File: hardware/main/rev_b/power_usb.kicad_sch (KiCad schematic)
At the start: 32 parts, among them J1 USB-C USB2, J2 ESC_CAN_POWER, U1 USBLC6-2SC6, U2 TLV62569DBVR, U3 TLV75528PDBVR, U4 TLV75533PDBVR

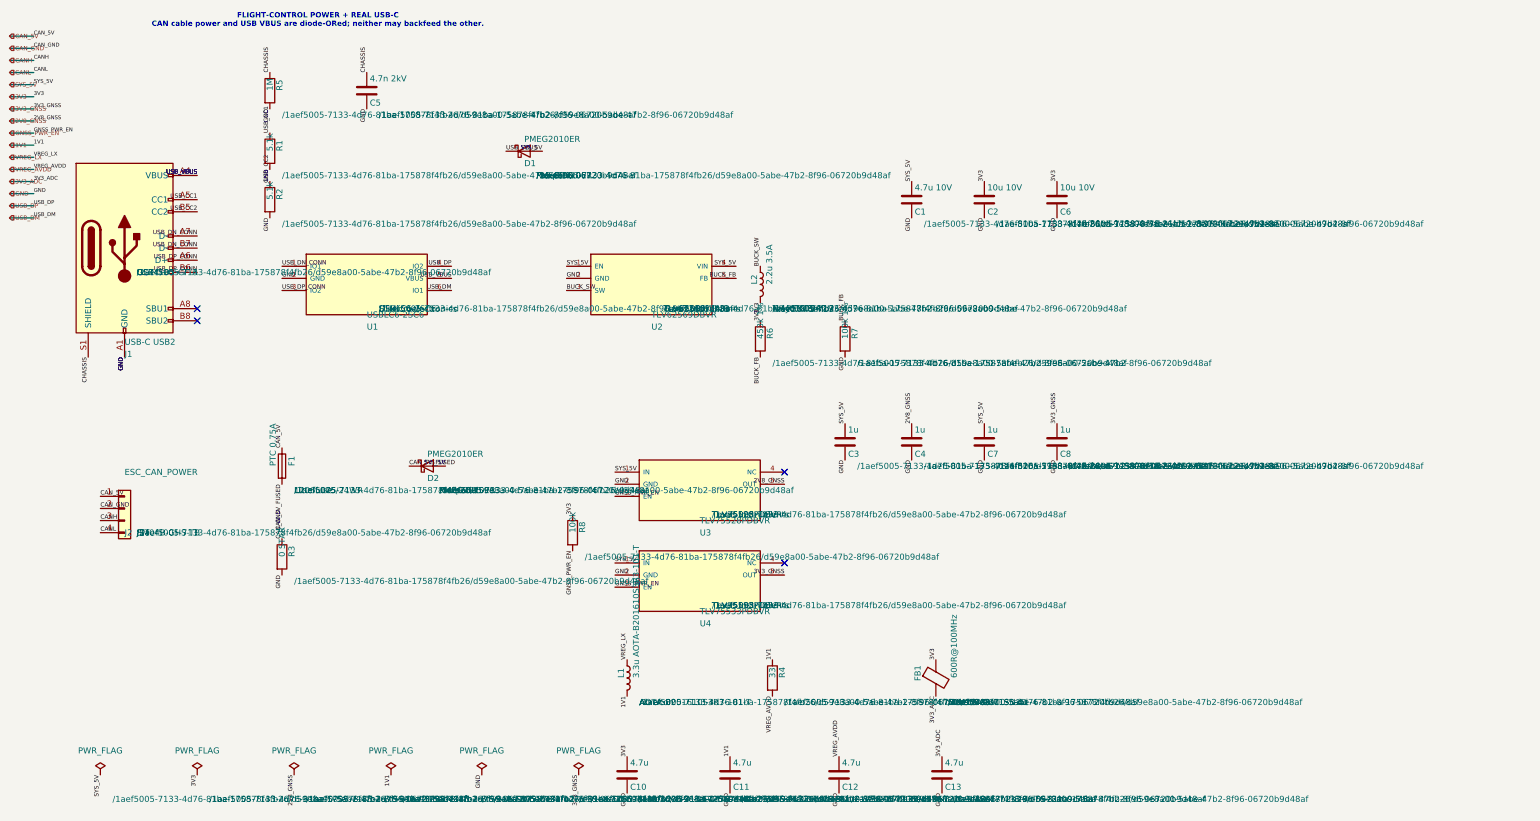
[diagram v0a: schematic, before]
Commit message: build: route and validate rev-b boards
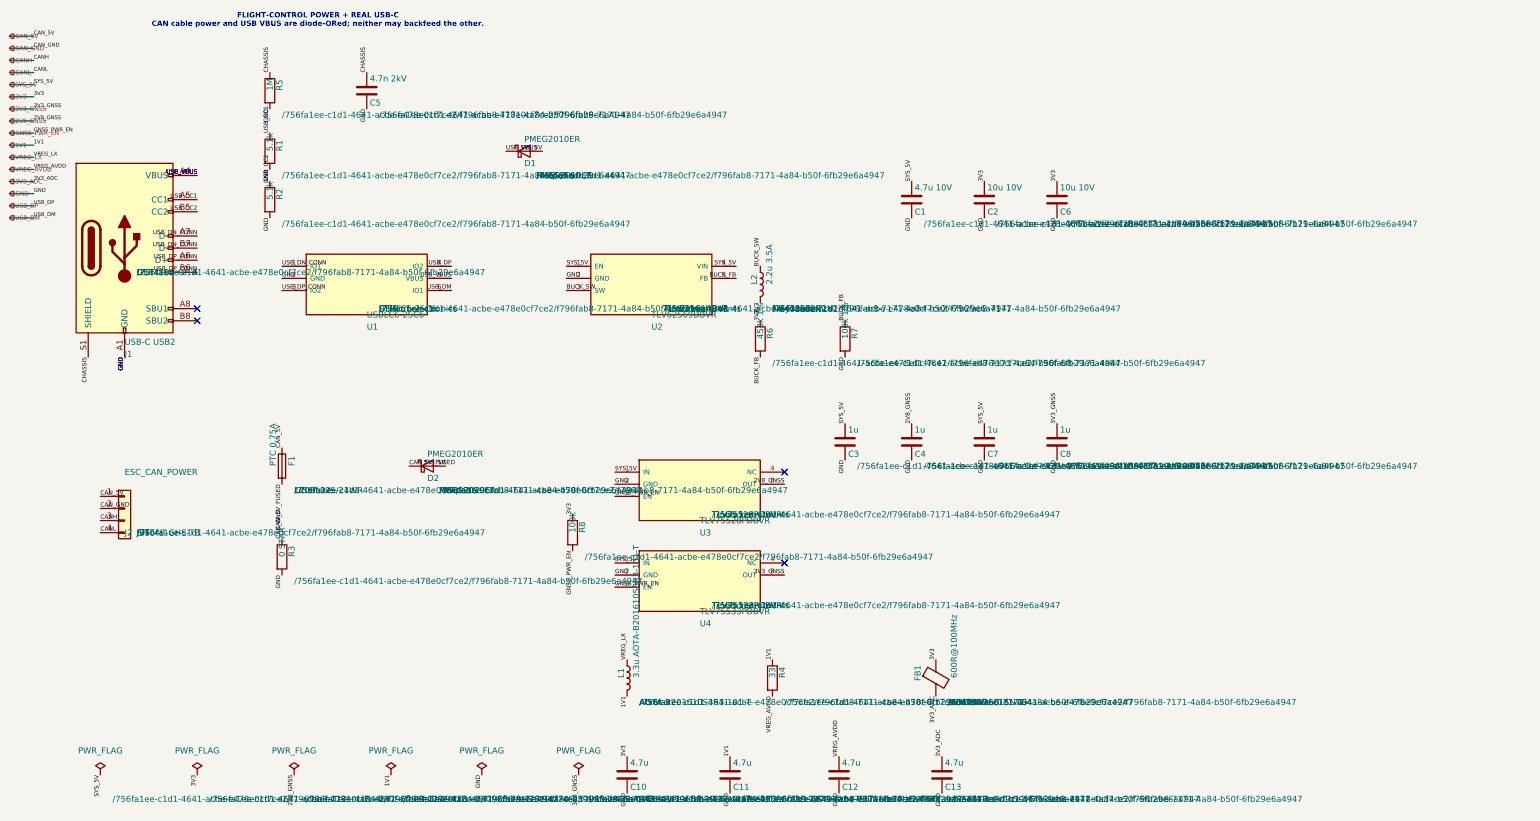
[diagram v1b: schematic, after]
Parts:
- C1, C10, C11, C12, C13, C2, C3, C4, C5, C6, C7, C8, D1, D2, F1, FB1, J1, J2, L1, L2, R1, R2, R3, R4, R5, R6, R7, R8, U1, U2, U3, U4: hierarchy_path /1aef5005-7133-4d76-81ba-175878f4fb26/d59e8a00-5abe-47b2-8f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 -> /756fa1ee-c1d1-4641-acbe-e478e0cf7ce2/f796fab8-7171-4a84-b5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

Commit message: build: route and validate rev-b boards
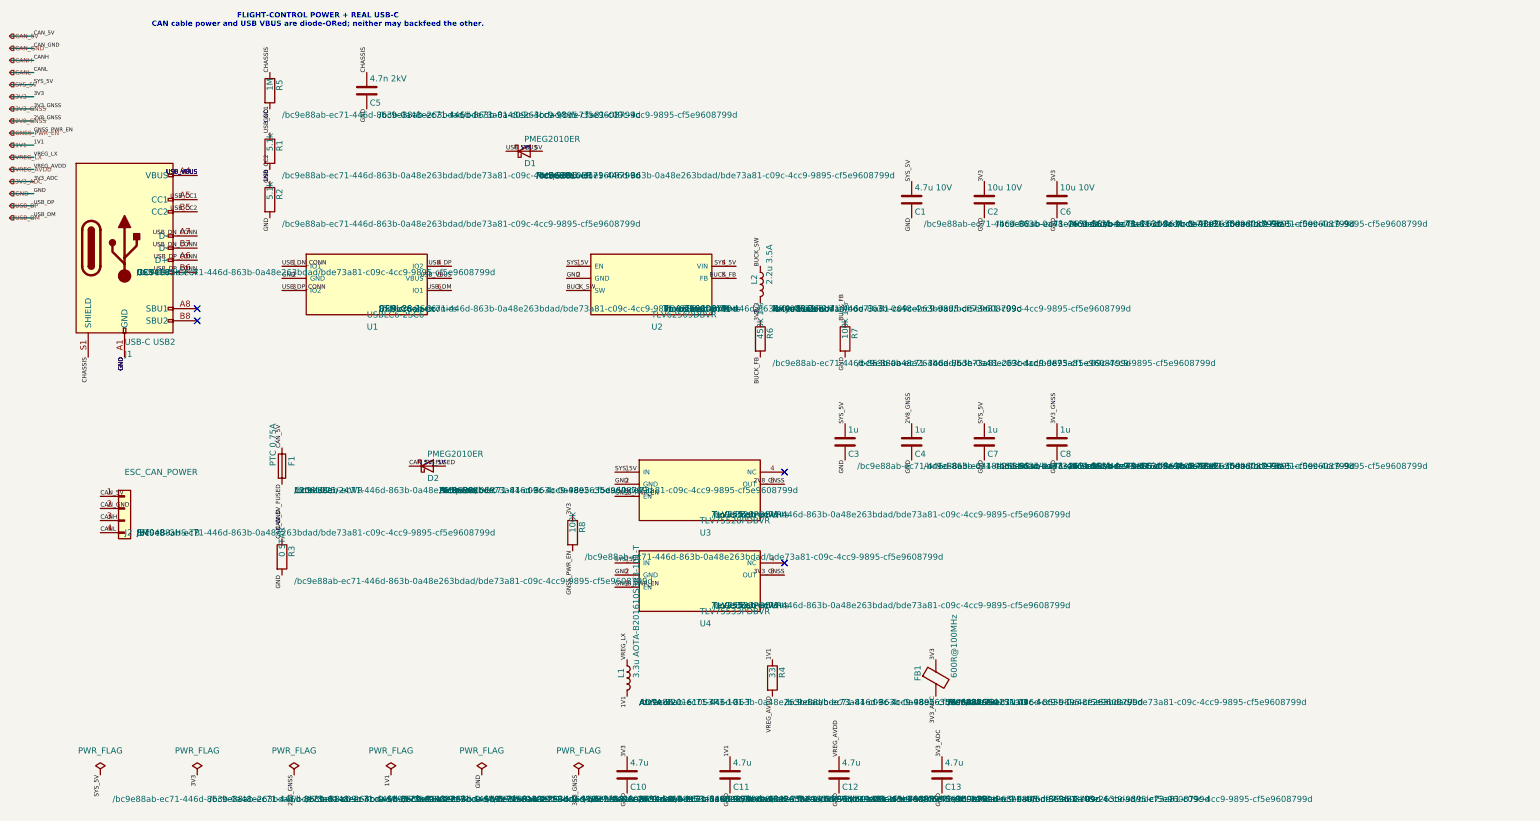
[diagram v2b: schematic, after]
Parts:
- C1, C10, C11, C12, C13, C2, C3, C4, C5, C6, C7, C8, D1, D2, F1, FB1, J1, J2, L1, L2, R1, R2, R3, R4, R5, R6, R7, R8, U1, U2, U3, U4: hierarchy_path /756fa1ee-c1d1-4641-acbe-e478e0cf7ce2/f796fab8-7171-4a84-b5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 -> /bc9e88ab-ec71-446d-863b-0a48e263bdad/bde73a81-c09c-4cc9-98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

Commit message: build: route and validate rev-b boards
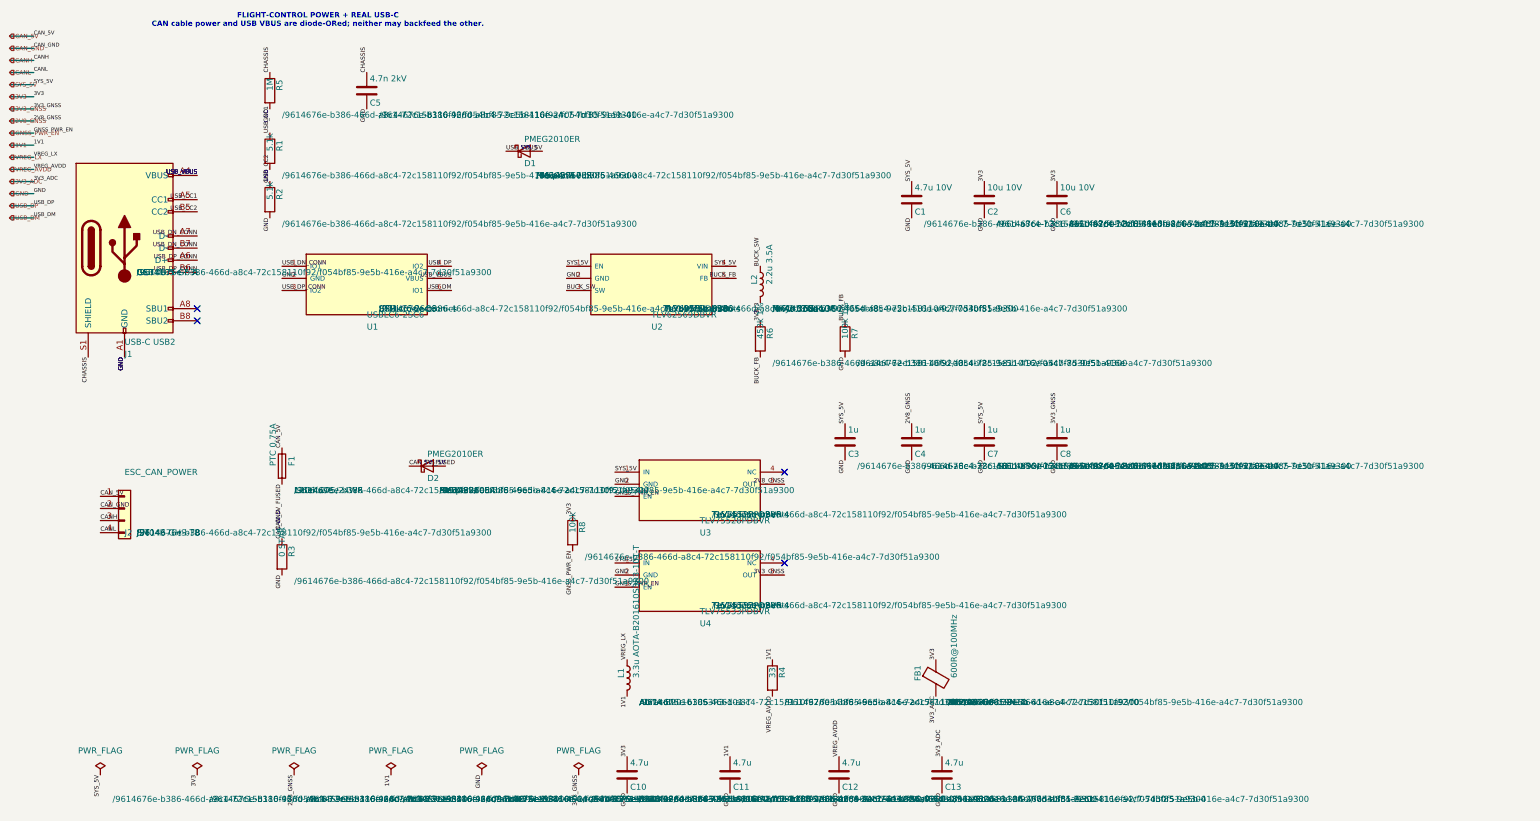
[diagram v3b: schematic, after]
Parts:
- C1, C10, C11, C12, C13, C2, C3, C4, C5, C6, C7, C8, D1, D2, F1, FB1, J1, J2, L1, L2, R1, R2, R3, R4, R5, R6, R7, R8, U1, U2, U3, U4: hierarchy_path /bc9e88ab-ec71-446d-863b-0a48e263bdad/bde73a81-c09c-4cc9-98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 -> /9614676e-b386-466d-a8c4-72c158110f92/f054bf85-9e5b-416e-a4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
